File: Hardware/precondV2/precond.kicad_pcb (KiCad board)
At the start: 2 copper layers, 92 x 96 mm, 47 parts, among them J1 Conn_Coaxial, J2 Conn_Coaxial, J3 XADC_header, J4 Screw_Terminal_01x03, J5 UART_hdr, Q1 IRLML6344TRPBF, Q2 IRLML9301TRPBF, U1 OPA2340, U2 OPA2340

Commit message: V2 of the PCB
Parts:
- moved TPCH2 3.10 mm to (101.0, 84.2)
- moved J2 1.59 mm to (98.9, 74.5)
- moved D2 0.95 mm to (94.6, 88.0)
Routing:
- net Net-(J2-In): track 14.4 -> 17.0 mm
- net Net-(D2-A1): track 7.93 -> 8.58 mm
- net AGND: vias 75 -> 84
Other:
- board text added: "Precondition Board"
- board text removed: "Preconditionificator 9000"

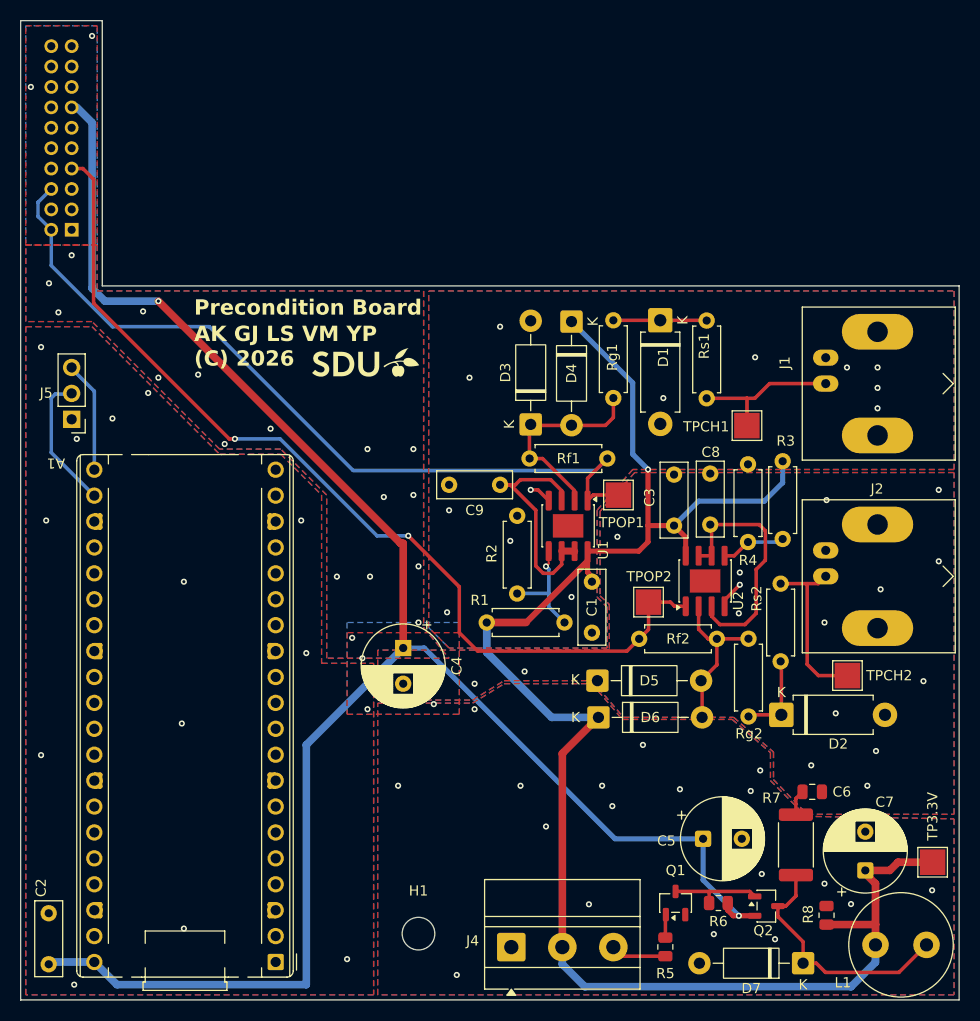
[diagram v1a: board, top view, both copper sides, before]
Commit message: added platform MHs
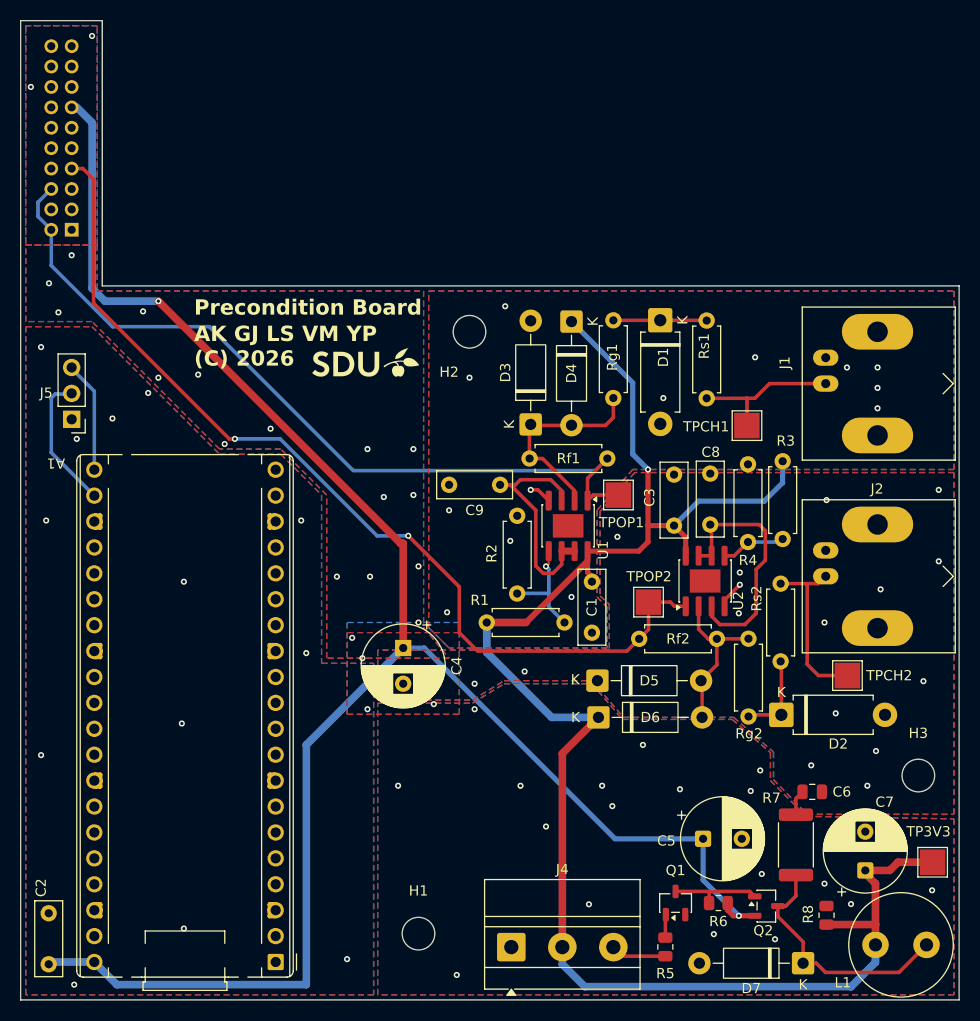
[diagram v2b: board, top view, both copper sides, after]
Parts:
- added H2: MountingHole, MountingHole:MountingHole_3.2mm_M3, F.Cu at (64.0, 50.5)
- added H3: MountingHole, MountingHole:MountingHole_3.2mm_M3, F.Cu at (108.0, 94.0)
- renumbered TP3.3V to TP3V3
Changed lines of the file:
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@@
 		(tags "THT terminal block Metz Connect Type011_RT05503HBLC pitch 5mm size 15x10.5mm drill 1.4mm pad 2.8mm")
 		(property "Reference" "J4"
-			(at -3.8 -0.6175 0)
+			(at 5 -7.62 0)
 			(layer "F.SilkS")
 			(effects
@@
 		(fp_line
 			(start -2.62 -6.62)
-			(end -2.62 4.12)
-			(stroke
-				(width 0.12)
-				(type solid)
-			)
-			(layer "F.SilkS")
-		)
-		(fp_line
-			(start -2.62 -6.62)
 			(end 12.62 -6.62)
 			(stroke
@@
 		(fp_line
 			(start -2.62 4.12)
-			(end -0.3 4.12)
+			(end -2.62 -6.62)
 			(stroke
 				(width 0.12)
@@
 		)
 		(fp_line
-			(start 0.3 4.12)
-			(end 12.62 4.12)
+			(start -0.3 4.12)
+			(end -2.62 4.12)
 			(stroke
 				(width 0.12)
@@
 			(layer "F.SilkS")
 		)
+		(fp_line
+			(start 12.62 4.12)
+			(end 0.3 4.12)
+			(stroke
+				(width 0.12)
+				(type solid)
+			)
+			(layer "F.SilkS")
+		)
 		(fp_poly
 			(pts
@@
 			(layer "F.SilkS")
 		)
-		(fp_line
+		(fp_rect
 			(start -3 -7)
-			(end -3 4.5)
-			(stroke
-				(width 0.05)
-				(type solid)
-			)
-			(layer "F.CrtYd")
-		)
-		(fp_line
-			(start -3 4.5)
 			(end 13 4.5)
 			(stroke
@@
 				(type solid)
 			)
-			(layer "F.CrtYd")
-		)
-		(fp_line
-			(start 13 -7)
-			(end -3 -7)
-			(stroke
-				(width 0.05)
-				(type solid)
-			)
-			(layer "F.CrtYd")
-		)
-		(fp_line
-			(start 13 4.5)
-			(end 13 -7)
-			(stroke
-				(width 0.05)
-				(type solid)
-			)
+			(fill no)
 			(layer "F.CrtYd")
 		)
@@
 		(embedded_fonts no)
 	)
+	(footprint "MountingHole:MountingHole_3.2mm_M3"
+		(layer "F.Cu")
+		(at 64 50.5)
+		(descr "Mounting Hole 3.2mm, M3, no annular, generated by kicad-footprint-generator mountinghole.py")
+		(tags "mountinghole M3")
+		(property "Reference" "H2"
+			(at -2 3.95 0)
+			(layer "F.SilkS")
+			(effects
+				(font
+					(size 1 1)
+					(thickness 0.15)
+				)
+			)
+		)
+		(property "Value" "MountingHole"
+			(at 0 4.15 0)
+			(layer "F.Fab")
+			(effects
+				(font
+					(size 1 1)
+					(thickness 0.15)
+				)
+			)
+		)
+		(property "Datasheet" "~"
+			(at 0 0 0)
+			(layer "F.Fab")
+			(hide yes)
+			(effects
+				(font
+					(size 1.27 1.27)
+					(thickness 0.15)
+				)
+			)
+		)
+		(property "Description" "Mounting Hole without connection"
+			(at 0 0 0)
+			(layer "F.Fab")
+			(hide yes)
+			(effects
+				(font
+					(size 1.27 1.27)
+					(thickness 0.15)
+				)
+			)
+		)
+		(property ki_fp_filters "MountingHole*")
+		(sheetname "/")
+		(sheetfile "precond.kicad_sch")
+		(attr exclude_from_pos_files exclude_from_bom)
+		(fp_circle
+			(center 0 0)
+			(end 3.2 0)
+			(stroke
+				(width 0.15)
+				(type solid)
+			)
+			(fill no)
+			(layer "Cmts.User")
+		)
+		(fp_circle
+			(center 0 0)
+			(end 3.45 0)
+			(stroke
+				(width 0.05)
+				(type solid)
+			)
+			(fill no)
+			(layer "F.CrtYd")
+		)
+		(fp_text user "${REFERENCE}"
+			(at 0 0 0)
+			(layer "F.Fab")
+			(effects
+				(font
+					(size 1 1)
+					(thickness 0.15)
+				)
+			)
+		)
+		(pad "" np_thru_hole circle
+			(at 0 0)
+			(size 3.2 3.2)
+			(drill 3.2)
+			(layers "*.Cu" "*.Mask")
+		)
+		(embedded_fonts no)
+	)
 	(footprint "Resistor_SMD:R_0805_2012Metric"
 		(layer "F.Cu")
@@
 		)
 	)
+	(footprint "MountingHole:MountingHole_3.2mm_M3"
+		(layer "F.Cu")
+		(at 108 94)
+		(descr "Mounting Hole 3.2mm, M3, no annular, generated by kicad-footprint-generator mountinghole.py")
+		(tags "mountinghole M3")
+		(property "Reference" "H3"
+			(at 0 -4.15 0)
+			(layer "F.SilkS")
+			(effects
+				(font
+					(size 1 1)
+					(thickness 0.15)
+				)
+			)
+		)
+		(property "Value" "MountingHole"
+			(at 0 4.15 0)
+			(layer "F.Fab")
+			(effects
+				(font
+					(size 1 1)
+					(thickness 0.15)
+				)
+			)
+		)
+		(property "Datasheet" "~"
+			(at 0 0 0)
+			(layer "F.Fab")
+			(hide yes)
+			(effects
+				(font
+					(size 1.27 1.27)
+					(thickness 0.15)
+				)
+			)
+		)
+		(property "Description" "Mounting Hole without connection"
+			(at 0 0 0)
+			(layer "F.Fab")
+			(hide yes)
+			(effects
+				(font
+					(size 1.27 1.27)
+					(thickness 0.15)
+				)
+			)
+		)
+		(property ki_fp_filters "MountingHole*")
+		(sheetname "/")
+		(sheetfile "precond.kicad_sch")
+		(attr exclude_from_pos_files exclude_from_bom)
+		(fp_circle
+			(center 0 0)
+			(end 3.2 0)
+			(stroke
+				(width 0.15)
+				(type solid)
+			)
+			(fill no)
+			(layer "Cmts.User")
+		)
+		(fp_circle
+			(center 0 0)
+			(end 3.45 0)
+			(stroke
+				(width 0.05)
+				(type solid)
+			)
+			(fill no)
+			(layer "F.CrtYd")
+		)
+		(fp_text user "${REFERENCE}"
+			(at 0 0 0)
+			(layer "F.Fab")
+			(effects
+				(font
+					(size 1 1)
+					(thickness 0.15)
+				)
+			)
+		)
+		(pad "" np_thru_hole circle
+			(at 0 0)
+			(size 3.2 3.2)
+			(drill 3.2)
+			(layers "*.Cu" "*.Mask")
+		)
+		(embedded_fonts no)
+	)
 	(footprint "Diode_THT:D_DO-41_SOD81_P10.16mm_Horizontal"
 		(layer "F.Cu")
@@
 		(descr "SMD rectangular pad as test Point, square 2.5mm side length")
 		(tags "test point SMD pad rectangle square")
-		(property "Reference" "TP3.3V"
-			(at -4.5 0 270)
+		(property "Reference" "TP3V3"
+			(at -3 0.4 0)
 			(layer "F.SilkS")
 			(effects
@@
 	)
 	(via
-		(at 67 50)
+		(at 67.5 48)
 		(size 0.6)
 		(drill 0.3)

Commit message: final pcb
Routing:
- net AGND: vias 84 -> 85
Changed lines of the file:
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@@
+	)
+	(via
+		(at 81.5 73)
+		(size 0.6)
+		(drill 0.3)
+		(layers "F.Cu" "B.Cu")
+		(free yes)
+		(net 36)
 	)
 	(via
@@
 	)
 	(via
-		(at 99 67)
+		(at 99 66)
 		(size 0.6)
 		(drill 0.3)
